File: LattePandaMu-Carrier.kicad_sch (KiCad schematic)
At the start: 6 parts

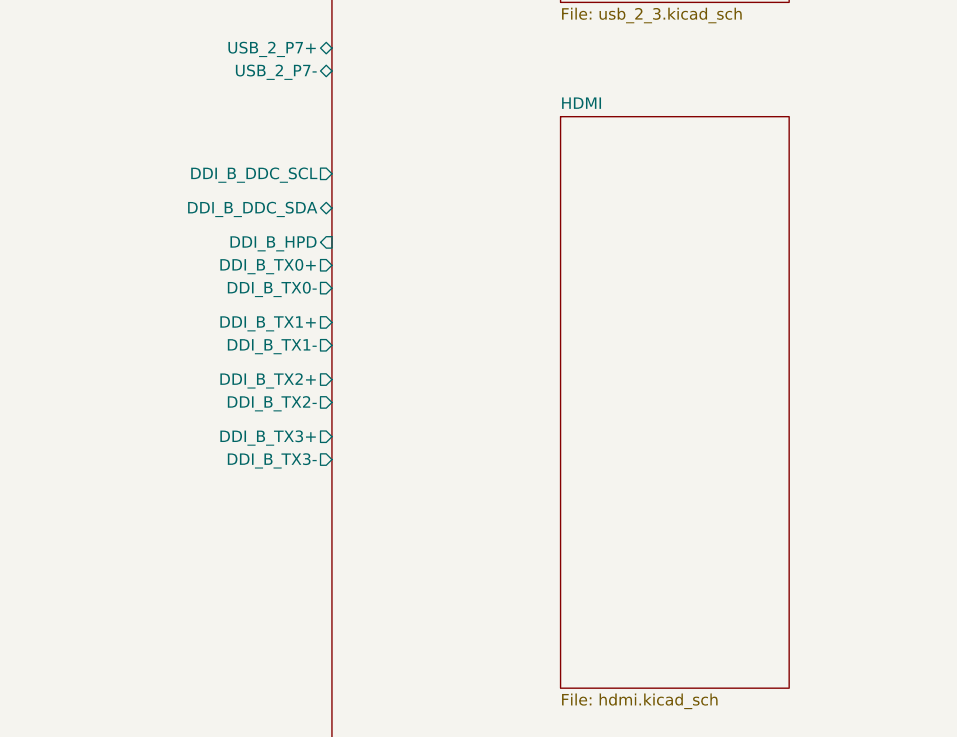
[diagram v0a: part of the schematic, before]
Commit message: feat(hdmi): Added HDMI implementation and connections.
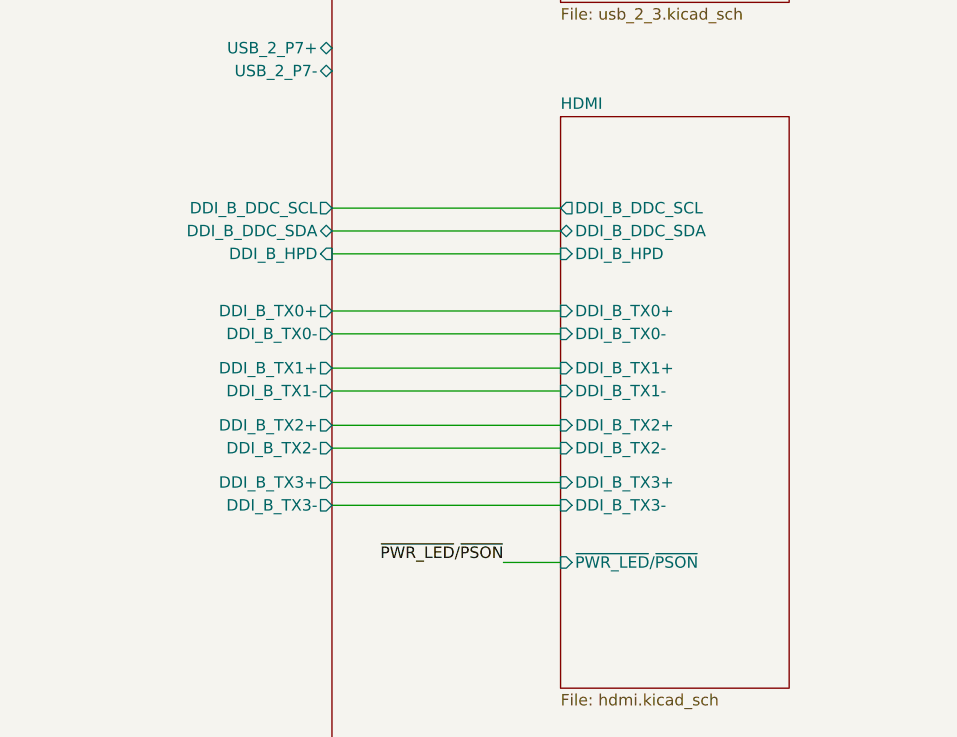
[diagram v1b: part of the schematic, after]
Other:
- sheet HDMI ports: added DDI_B_DDC_SCL, DDI_B_DDC_SDA, DDI_B_HPD, DDI_B_TX0+, DDI_B_TX0-, DDI_B_TX1+, DDI_B_TX1-, DDI_B_TX2+, DDI_B_TX2-, DDI_B_TX3+, DDI_B_TX3-, ~{PWR_LED}/~{PSON}; removed none

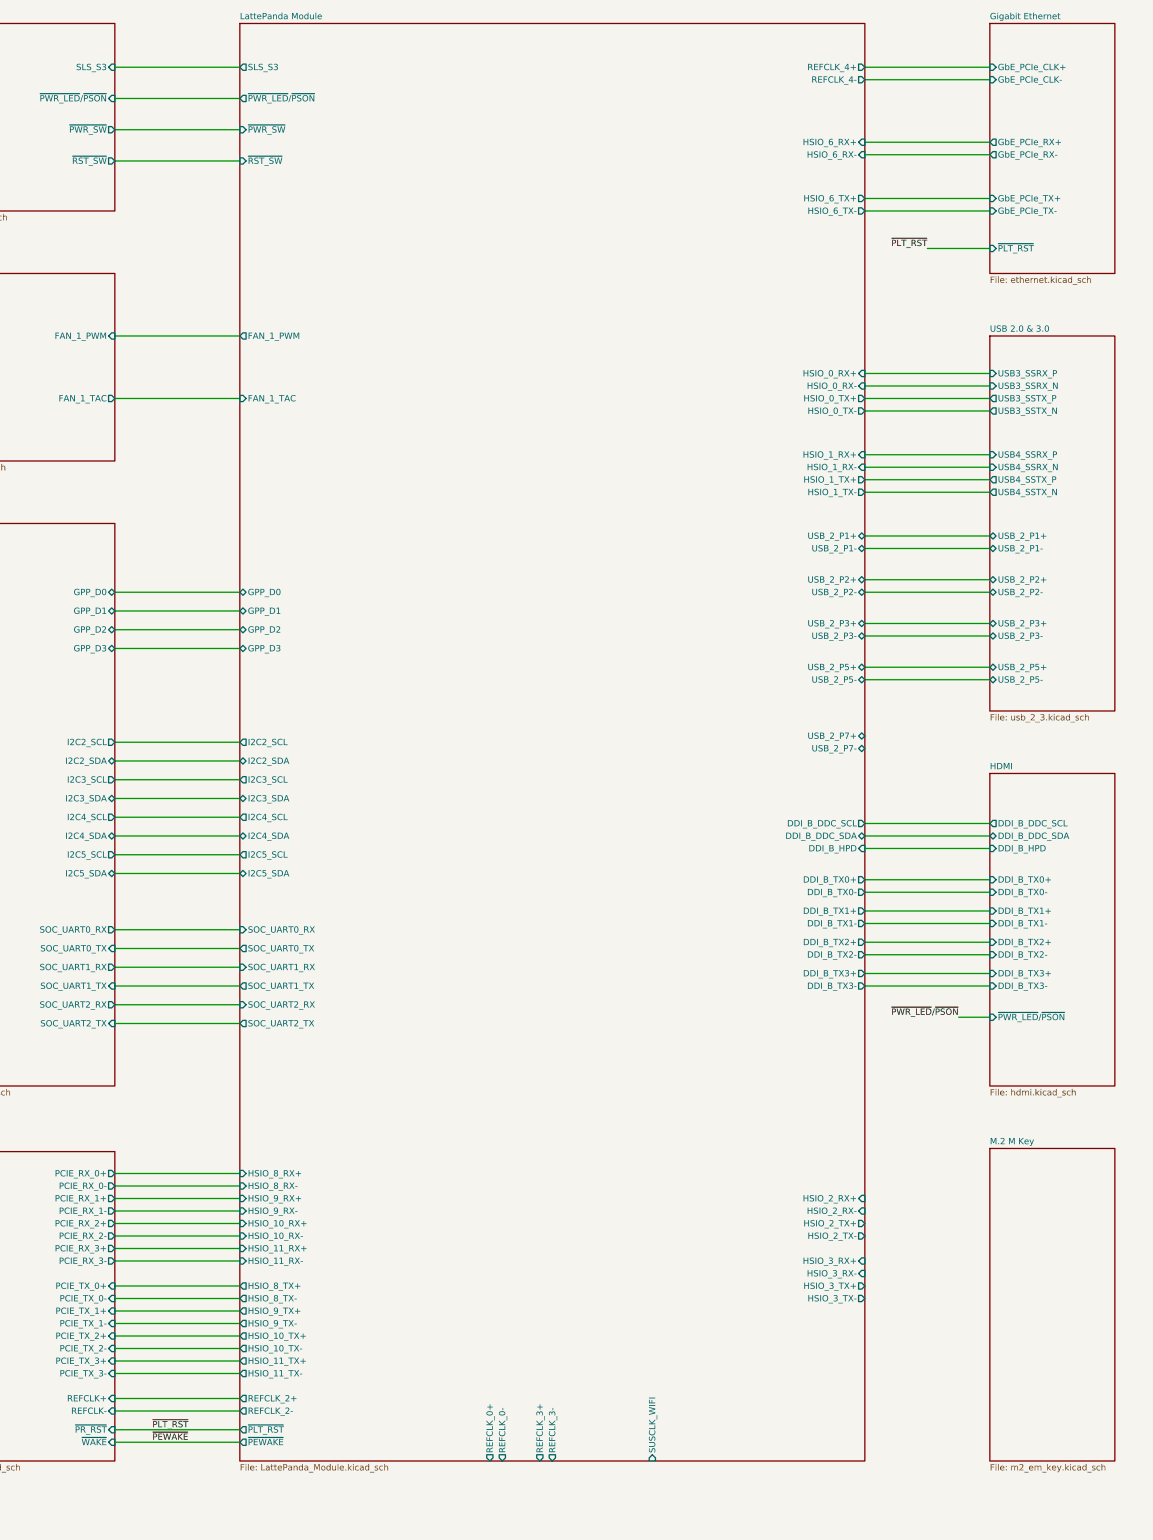
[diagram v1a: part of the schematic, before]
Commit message: feat(m.2): Added m.2 E and M keys
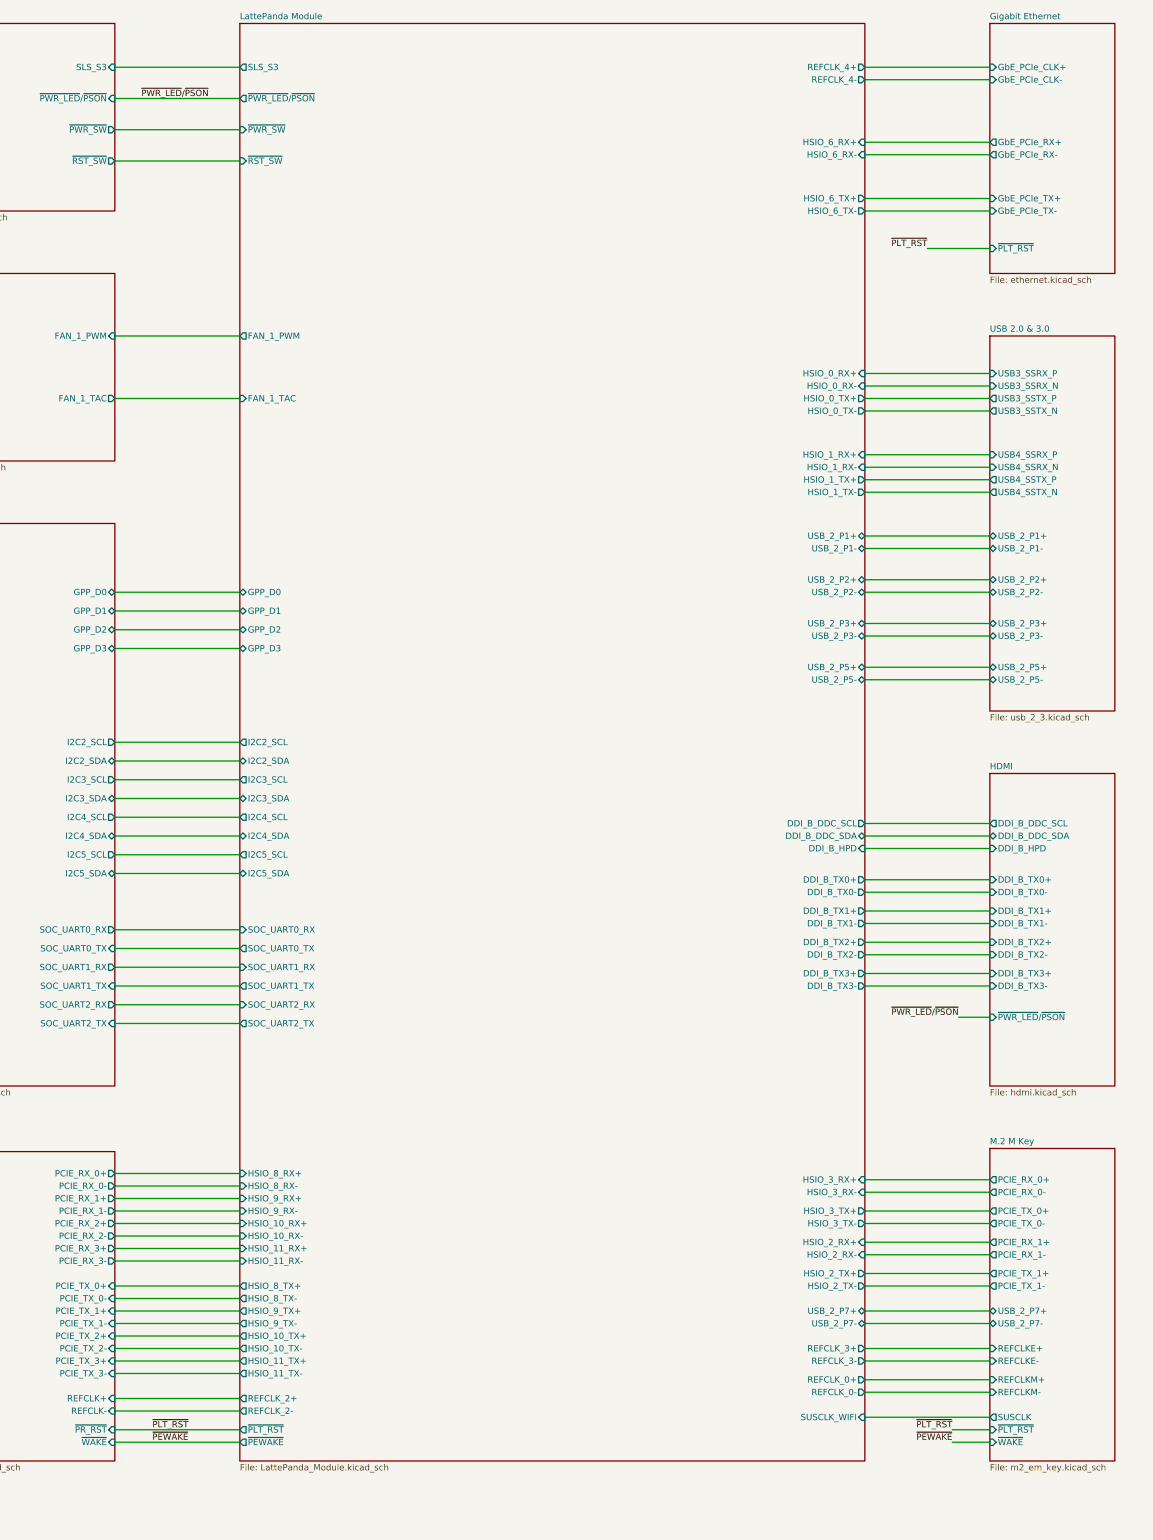
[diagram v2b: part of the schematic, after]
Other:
- sheet M.2 M Key ports: added PCIE_RX_0+, PCIE_RX_0-, PCIE_RX_1+, PCIE_RX_1-, PCIE_TX_0+, PCIE_TX_0-, PCIE_TX_1+, PCIE_TX_1-, REFCLKE+, REFCLKE-, REFCLKM+, REFCLKM-, SUSCLK, USB_2_P7+, USB_2_P7-, ~{PLT_RST}, ~{WAKE}; removed none

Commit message: fix: Set missing footprints and fixed missing pin-pad connections.
- J15, J16 missing MP1 and MP2 pins. Fixed in pin table within the symbol editor for each symbol.
- A ll USB receptacles J4, J5, J18 had mismatched pin numbers for the pcb symbol footprint. Renamed to match.
- Fixed various DNP components that were not excluded from the board.
- Fixed remaining missing footprints.
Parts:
- FID78, FID79: footprint (none) -> A_HDJ_Library:Fiducial_0.5mm_Mask1mm
- H1, H2, H3, H4: footprint (none) -> A_HDJ_Library:MountingHole_3.2mm_M3_Pad_Via
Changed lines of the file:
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@@
 			)
 		)
-		(property "Footprint" ""
+		(property "Footprint" "A_HDJ_Library:MountingHole_3.2mm_M3_Pad_Via"
 			(at 496.57 318.77 0)
 			(hide yes)
@@
 		)
 		(property "Description" "Mounting Hole with connection"
+			(at 496.57 318.77 0)
+			(hide yes)
+			(show_name no)
+			(do_not_autoplace no)
+			(effects
+				(font
+					(size 1.27 1.27)
+				)
+			)
+		)
+		(property "KLC_S3.3" ""
+			(at 496.57 318.77 0)
+			(hide yes)
+			(show_name no)
+			(do_not_autoplace no)
+			(effects
+				(font
+					(size 1.27 1.27)
+				)
+			)
+		)
+		(property "KLC_S4.1" ""
 			(at 496.57 318.77 0)
 			(hide yes)
@@
 			)
 		)
-		(property "Footprint" ""
+		(property "Footprint" "A_HDJ_Library:Fiducial_0.5mm_Mask1mm"
 			(at 496.57 354.33 0)
 			(hide yes)
@@
 		)
 		(property "Description" "Fiducial Marker"
+			(at 496.57 354.33 0)
+			(hide yes)
+			(show_name no)
+			(do_not_autoplace no)
+			(effects
+				(font
+					(size 1.27 1.27)
+				)
+			)
+		)
+		(property "KLC_S3.3" ""
+			(at 496.57 354.33 0)
+			(hide yes)
+			(show_name no)
+			(do_not_autoplace no)
+			(effects
+				(font
+					(size 1.27 1.27)
+				)
+			)
+		)
+		(property "KLC_S4.1" ""
 			(at 496.57 354.33 0)
 			(hide yes)
@@
 			)
 		)
-		(property "Footprint" ""
+		(property "Footprint" "A_HDJ_Library:Fiducial_0.5mm_Mask1mm"
 			(at 534.67 354.33 0)
 			(hide yes)
@@
 		)
 		(property "Description" "Fiducial Marker"
+			(at 534.67 354.33 0)
+			(hide yes)
+			(show_name no)
+			(do_not_autoplace no)
+			(effects
+				(font
+					(size 1.27 1.27)
+				)
+			)
+		)
+		(property "KLC_S3.3" ""
+			(at 534.67 354.33 0)
+			(hide yes)
+			(show_name no)
+			(do_not_autoplace no)
+			(effects
+				(font
+					(size 1.27 1.27)
+				)
+			)
+		)
+		(property "KLC_S4.1" ""
 			(at 534.67 354.33 0)
 			(hide yes)
@@
 			)
 		)
-		(property "Footprint" ""
+		(property "Footprint" "A_HDJ_Library:MountingHole_3.2mm_M3_Pad_Via"
 			(at 496.57 336.55 0)
 			(hide yes)
@@
 		)
 		(property "Description" "Mounting Hole with connection"
+			(at 496.57 336.55 0)
+			(hide yes)
+			(show_name no)
+			(do_not_autoplace no)
+			(effects
+				(font
+					(size 1.27 1.27)
+				)
+			)
+		)
+		(property "KLC_S3.3" ""
+			(at 496.57 336.55 0)
+			(hide yes)
+			(show_name no)
+			(do_not_autoplace no)
+			(effects
+				(font
+					(size 1.27 1.27)
+				)
+			)
+		)
+		(property "KLC_S4.1" ""
 			(at 496.57 336.55 0)
 			(hide yes)
@@
 			)
 		)
-		(property "Footprint" ""
+		(property "Footprint" "A_HDJ_Library:MountingHole_3.2mm_M3_Pad_Via"
 			(at 534.67 336.55 0)
 			(hide yes)
@@
 		)
 		(property "Description" "Mounting Hole with connection"
+			(at 534.67 336.55 0)
+			(hide yes)
+			(show_name no)
+			(do_not_autoplace no)
+			(effects
+				(font
+					(size 1.27 1.27)
+				)
+			)
+		)
+		(property "KLC_S3.3" ""
+			(at 534.67 336.55 0)
+			(hide yes)
+			(show_name no)
+			(do_not_autoplace no)
+			(effects
+				(font
+					(size 1.27 1.27)
+				)
+			)
+		)
+		(property "KLC_S4.1" ""
 			(at 534.67 336.55 0)
 			(hide yes)
@@
 			)
 		)
-		(property "Footprint" ""
+		(property "Footprint" "A_HDJ_Library:MountingHole_3.2mm_M3_Pad_Via"
 			(at 534.67 318.77 0)
 			(hide yes)
@@
 			(at 534.67 318.77 0)
 			(hide yes)
+			(show_name no)
+			(do_not_autoplace no)
+			(effects
+				(font
+					(size 1.27 1.27)
+				)
+			)
+		)
+		(property "KLC_S3.3" ""
+			(at 534.67 318.77 0)
+			(hide yes)
+			(show_name no)
+			(do_not_autoplace no)
+			(effects
+				(font
+					(size 1.27 1.27)
+				)
+			)
+		)
+		(property "KLC_S4.1" ""
+			(at 534.67 318.77 0)
+			(hide yes)
